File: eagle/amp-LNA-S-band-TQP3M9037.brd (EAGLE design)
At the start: 25 x 20 mm, 18 parts, among them J1 142-0701-851, J2 142-0701-851, U1 TQP3M903X

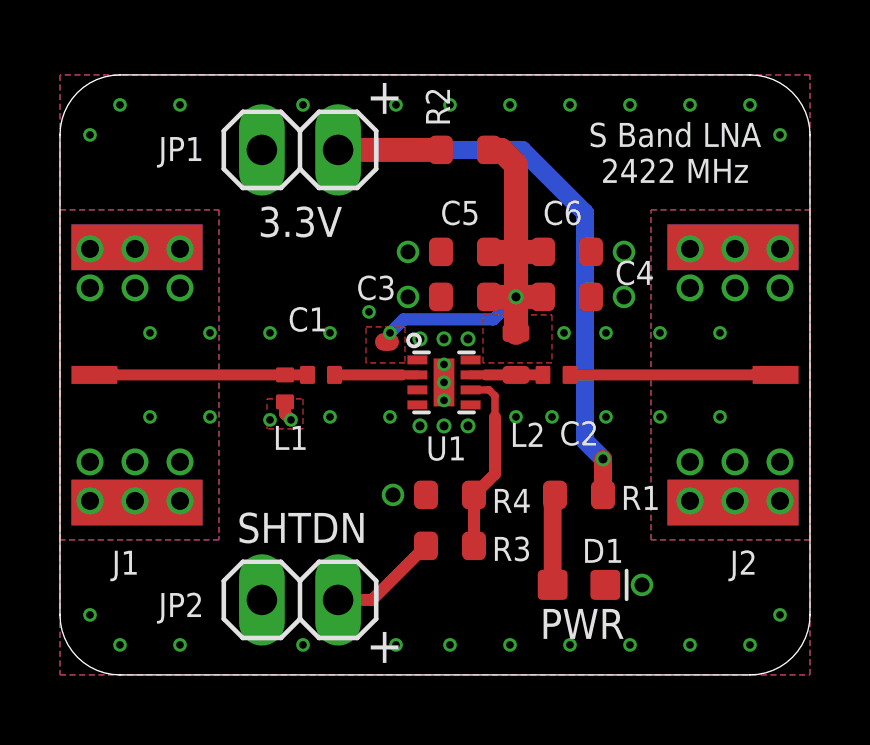
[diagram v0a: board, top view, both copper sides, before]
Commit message: Change SMA via sizes
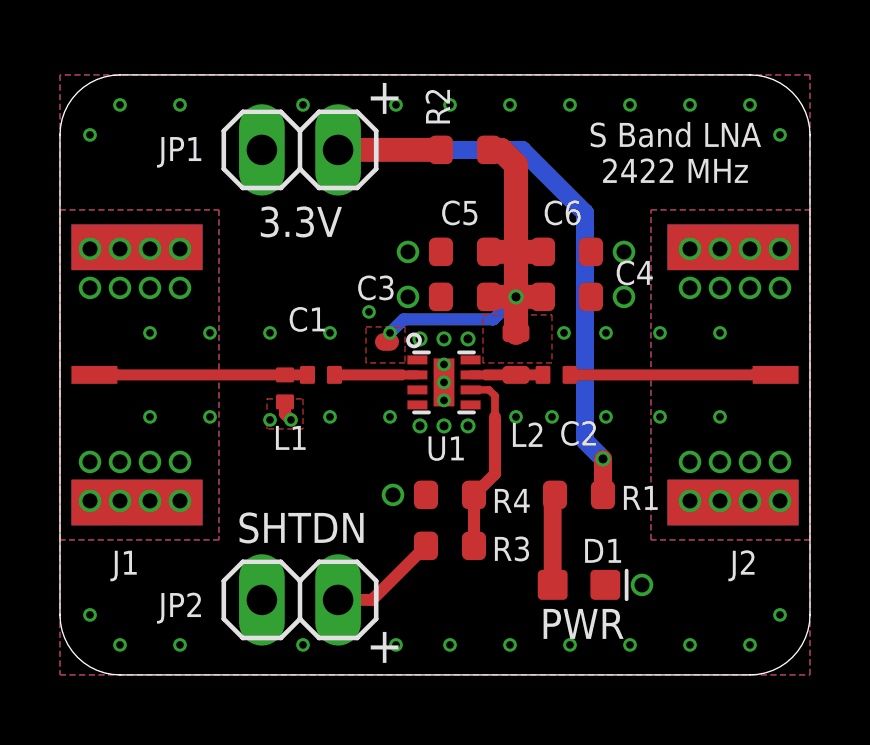
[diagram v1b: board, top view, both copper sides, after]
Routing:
- net GND: vias 83 -> 91
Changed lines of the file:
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@@
 <drawing>
 <settings>
-<setting alwaysvectorfont="yes"/>
+<setting alwaysvectorfont="no"/>
 <setting verticaltext="up"/>
 </settings>
@@
 <vertex x="0" y="20"/>
 </polygon>
-<via x="1" y="7.1" extent="1-16" drill="0.6"/>
-<via x="2.5" y="7.1" extent="1-16" drill="0.6"/>
-<via x="4" y="7.1" extent="1-16" drill="0.6"/>
-<via x="1" y="5.8" extent="1-16" drill="0.6"/>
-<via x="2.5" y="5.8" extent="1-16" drill="0.6"/>
-<via x="4" y="5.8" extent="1-16" drill="0.6"/>
-<via x="1" y="12.9" extent="1-16" drill="0.6"/>
-<via x="2.5" y="12.9" extent="1-16" drill="0.6"/>
-<via x="4" y="12.9" extent="1-16" drill="0.6"/>
-<via x="1" y="14.2" extent="1-16" drill="0.6"/>
-<via x="2.5" y="14.2" extent="1-16" drill="0.6"/>
-<via x="4" y="14.2" extent="1-16" drill="0.6"/>
-<via x="24" y="14.2" extent="1-16" drill="0.6"/>
-<via x="22.5" y="14.2" extent="1-16" drill="0.6"/>
-<via x="21" y="14.2" extent="1-16" drill="0.6"/>
-<via x="21" y="12.9" extent="1-16" drill="0.6"/>
-<via x="22.5" y="12.9" extent="1-16" drill="0.6"/>
-<via x="24" y="12.9" extent="1-16" drill="0.6"/>
-<via x="24" y="5.8" extent="1-16" drill="0.6"/>
-<via x="22.5" y="5.8" extent="1-16" drill="0.6"/>
-<via x="21" y="5.8" extent="1-16" drill="0.6"/>
-<via x="21" y="7.1" extent="1-16" drill="0.6"/>
-<via x="22.5" y="7.1" extent="1-16" drill="0.6"/>
-<via x="24" y="7.1" extent="1-16" drill="0.6"/>
+<via x="1" y="7.1" extent="1-16" drill="0.5"/>
+<via x="2" y="7.1" extent="1-16" drill="0.5"/>
+<via x="4" y="7.1" extent="1-16" drill="0.5"/>
+<via x="1" y="5.8" extent="1-16" drill="0.5"/>
+<via x="2" y="5.8" extent="1-16" drill="0.5"/>
+<via x="4" y="5.8" extent="1-16" drill="0.5"/>
+<via x="1" y="12.9" extent="1-16" drill="0.5"/>
+<via x="2" y="12.9" extent="1-16" drill="0.5"/>
+<via x="4" y="12.9" extent="1-16" drill="0.5"/>
+<via x="1" y="14.2" extent="1-16" drill="0.5"/>
+<via x="2" y="14.2" extent="1-16" drill="0.5"/>
+<via x="4" y="14.2" extent="1-16" drill="0.5"/>
+<via x="24" y="14.2" extent="1-16" drill="0.5"/>
+<via x="23" y="14.2" extent="1-16" drill="0.5"/>
+<via x="21" y="14.2" extent="1-16" drill="0.5"/>
+<via x="21" y="12.9" extent="1-16" drill="0.5"/>
+<via x="23" y="12.9" extent="1-16" drill="0.5"/>
+<via x="24" y="12.9" extent="1-16" drill="0.5"/>
+<via x="24" y="5.8" extent="1-16" drill="0.5"/>
+<via x="23" y="5.8" extent="1-16" drill="0.5"/>
+<via x="21" y="5.8" extent="1-16" drill="0.5"/>
+<via x="21" y="7.1" extent="1-16" drill="0.5"/>
+<via x="23" y="7.1" extent="1-16" drill="0.5"/>
+<via x="24" y="7.1" extent="1-16" drill="0.5"/>
 <via x="3" y="8.6" extent="1-16" drill="0.254"/>
 <via x="5" y="8.6" extent="1-16" drill="0.254"/>
@@
 <wire x1="7.5" y1="9.1" x2="7.5" y2="8.7" width="0.4" layer="1"/>
 <wire x1="7.5" y1="8.7" x2="7.7" y2="8.5" width="0.4" layer="1"/>
+<via x="3" y="12.9" extent="1-16" drill="0.5"/>
+<via x="3" y="14.2" extent="1-16" drill="0.5"/>
+<via x="3" y="7.1" extent="1-16" drill="0.5"/>
+<via x="3" y="5.8" extent="1-16" drill="0.5"/>
+<via x="22" y="7.1" extent="1-16" drill="0.5"/>
+<via x="22" y="5.8" extent="1-16" drill="0.5"/>
+<via x="22" y="12.9" extent="1-16" drill="0.5"/>
+<via x="22" y="14.2" extent="1-16" drill="0.5"/>
 </signal>
 <signal name="N$28" class="1">

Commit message: Update SMA footprint
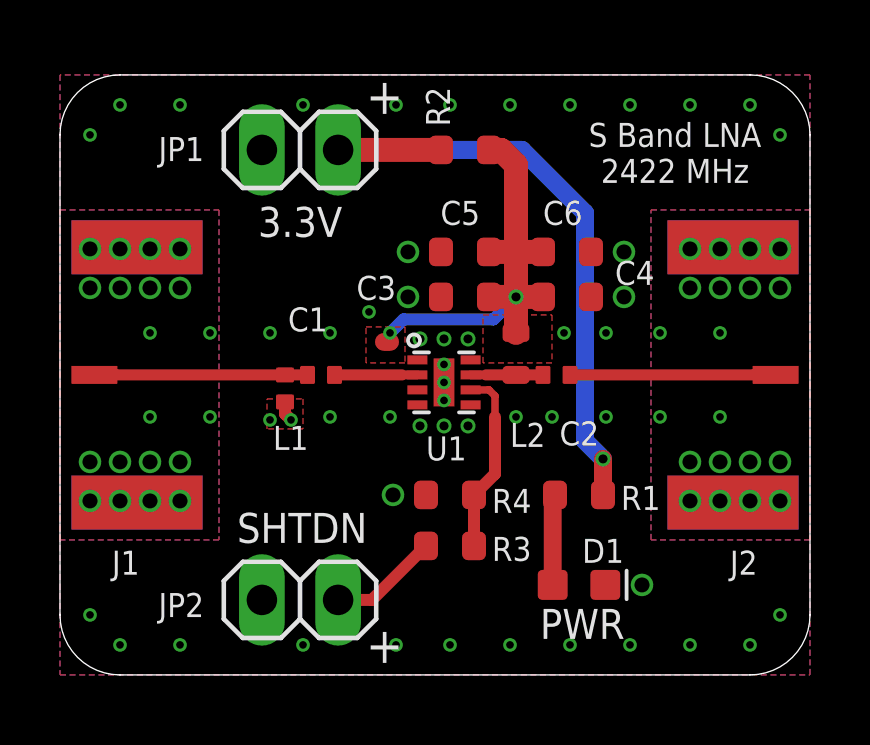
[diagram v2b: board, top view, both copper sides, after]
